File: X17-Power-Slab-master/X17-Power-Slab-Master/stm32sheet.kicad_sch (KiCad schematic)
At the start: 18 parts, among them J1 61201021621, SW2 1825910-6, U4 STM32F091CCTx, U7 ABLS-8.000MHZ-B2-T

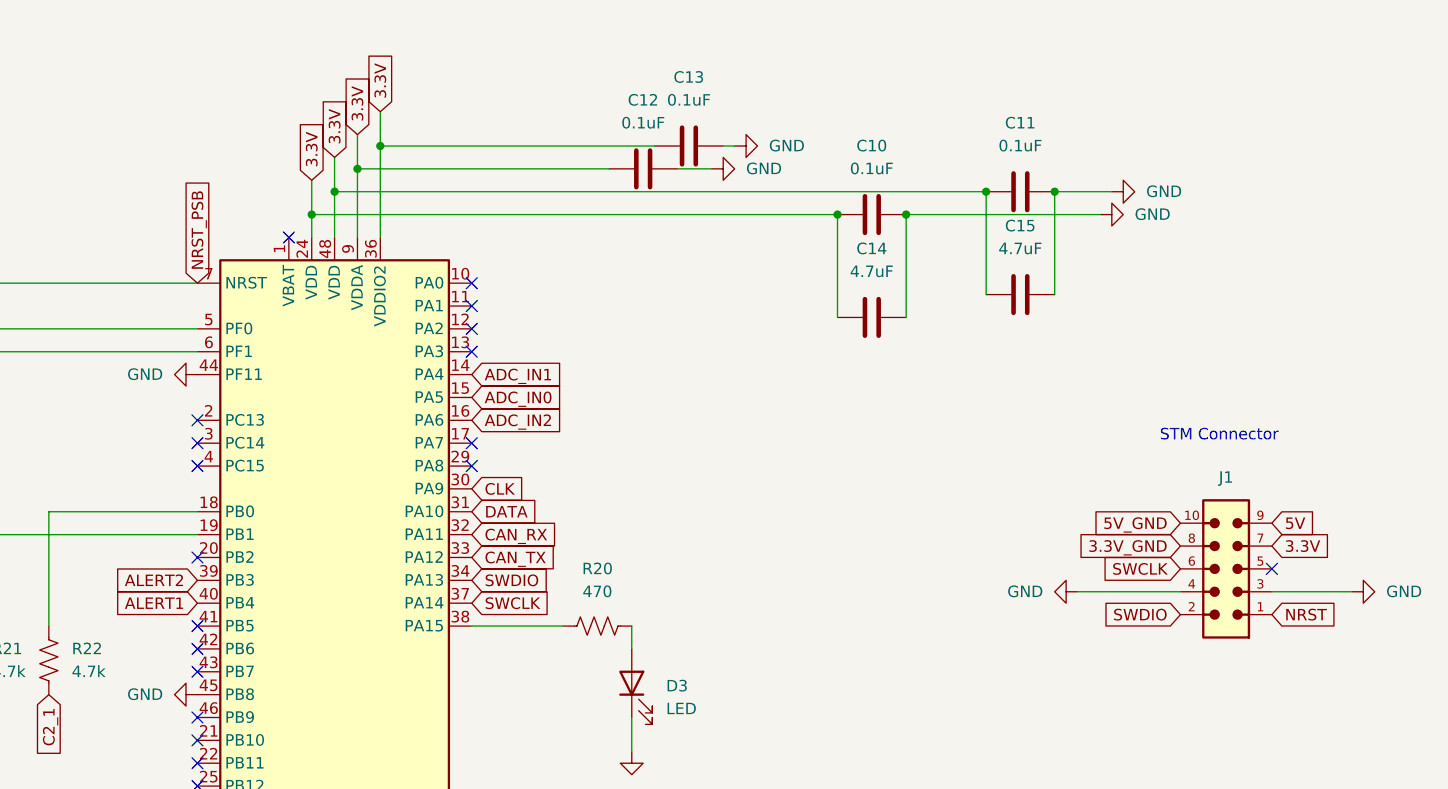
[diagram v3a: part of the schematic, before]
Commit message: Final First(?) Draft
NRST is stuck to general ground for whatever reason.

Test points wont connect for the life of me, will look @ in morning, will have sample plan.

Idea is there, really want to plan it out better 2nd time around. Alumni will give good tips!
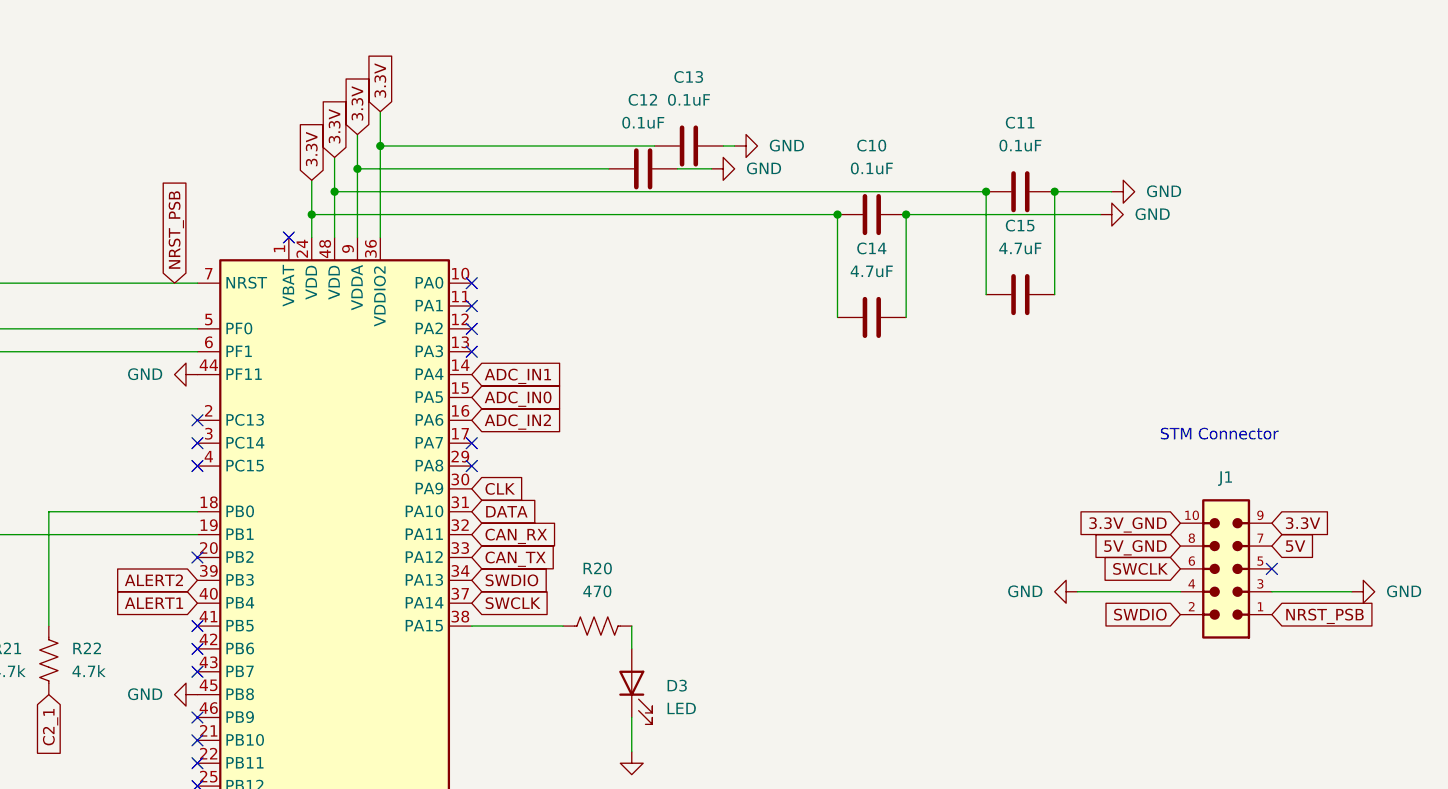
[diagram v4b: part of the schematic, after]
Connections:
- net NRST is gone; now on net GND: J1.1
- net 3.3V: now also J1.9; no longer J1.7
- net 3.3V_GND: now also J1.10; no longer J1.8
- net 5V: now also J1.7; no longer J1.9
- net 5V_GND: now also J1.8; no longer J1.10
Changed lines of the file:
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@@
 	(global_label "NRST_PSB"
 		(shape input)
-		(at 123.19 102.87 90)
-		(fields_autoplaced yes)
-		(effects
-			(font
-				(size 1.27 1.27)
-			)
-			(justify left)
-		)
-		(property "Intersheetrefs" "${INTERSHEET_REFS}"
-			(at 123.19 90.3901 90)
+		(at 120.65 102.87 90)
+		(fields_autoplaced yes)
+		(effects
+			(font
+				(size 1.27 1.27)
+			)
+			(justify left)
+		)
+		(property "Intersheetrefs" "${INTERSHEET_REFS}"
+			(at 120.65 90.3901 90)
 			(effects
 				(font
@@
 		)
 	)
+	(global_label "3.3V_GND"
+		(shape input)
+		(at 232.41 129.54 180)
+		(fields_autoplaced yes)
+		(effects
+			(font
+				(size 1.27 1.27)
+			)
+			(justify right)
+		)
+		(property "Intersheetrefs" "${INTERSHEET_REFS}"
+			(at 220.4743 129.54 0)
+			(effects
+				(font
+					(size 1.27 1.27)
+				)
+				(justify right)
+				(hide yes)
+			)
+		)
+	)
 	(global_label "5V_GND"
 		(shape input)
-		(at 232.41 129.54 180)
-		(fields_autoplaced yes)
-		(effects
-			(font
-				(size 1.27 1.27)
-			)
-			(justify right)
-		)
-		(property "Intersheetrefs" "${INTERSHEET_REFS}"
-			(at 222.2886 129.54 0)
-			(effects
-				(font
-					(size 1.27 1.27)
-				)
-				(justify right)
-				(hide yes)
-			)
-		)
-	)
-	(global_label "3.3V_GND"
-		(shape input)
 		(at 232.41 132.08 180)
 		(fields_autoplaced yes)
@@
 		)
 		(property "Intersheetrefs" "${INTERSHEET_REFS}"
-			(at 220.4743 132.08 0)
+			(at 222.2886 132.08 0)
 			(effects
 				(font
@@
 		)
 	)
-	(global_label "NRST"
+	(global_label "NRST_PSB"
 		(shape input)
 		(at 242.57 139.7 0)
@@
 		)
 		(property "Intersheetrefs" "${INTERSHEET_REFS}"
-			(at 250.3328 139.7 0)
+			(at 255.0499 139.7 0)
 			(effects
 				(font
@@
 		)
 	)
+	(global_label "3.3V"
+		(shape input)
+		(at 242.57 129.54 0)
+		(fields_autoplaced yes)
+		(effects
+			(font
+				(size 1.27 1.27)
+			)
+			(justify left)
+		)
+		(property "Intersheetrefs" "${INTERSHEET_REFS}"
+			(at 249.6676 129.54 0)
+			(effects
+				(font
+					(size 1.27 1.27)
+				)
+				(justify left)
+				(hide yes)
+			)
+		)
+	)
+	(global_label "3.3V"
+		(shape input)
+		(at 143.51 83.82 90)
+		(fields_autoplaced yes)
+		(effects
+			(font
+				(size 1.27 1.27)
+			)
+			(justify left)
+		)
+		(property "Intersheetrefs" "${INTERSHEET_REFS}"
+			(at 143.51 76.7224 90)
+			(effects
+				(font
+					(size 1.27 1.27)
+				)
+				(justify left)
+				(hide yes)
+			)
+		)
+	)
+	(global_label "3.3V"
+		(shape input)
+		(at 140.97 86.36 90)
+		(fields_autoplaced yes)
+		(effects
+			(font
+				(size 1.27 1.27)
+			)
+			(justify left)
+		)
+		(property "Intersheetrefs" "${INTERSHEET_REFS}"
+			(at 140.97 79.2624 90)
+			(effects
+				(font
+					(size 1.27 1.27)
+				)
+				(justify left)
+				(hide yes)
+			)
+		)
+	)
+	(global_label "ADC_IN0"
+		(shape input)
+		(at 153.67 115.57 0)
+		(fields_autoplaced yes)
+		(effects
+			(font
+				(size 1.27 1.27)
+			)
+			(justify left)
+		)
+		(property "Intersheetrefs" "${INTERSHEET_REFS}"
+			(at 164.3962 115.57 0)
+			(effects
+				(font
+					(size 1.27 1.27)
+				)
+				(justify left)
+				(hide yes)
+			)
+		)
+	)
+	(global_label "CAN_RX"
+		(shape input)
+		(at 153.67 130.81 0)
+		(fields_autoplaced yes)
+		(effects
+			(font
+				(size 1.27 1.27)
+			)
+			(justify left)
+		)
+		(property "Intersheetrefs" "${INTERSHEET_REFS}"
+			(at 163.7914 130.81 0)
+			(effects
+				(font
+					(size 1.27 1.27)
+				)
+				(justify left)
+				(hide yes)
+			)
+		)
+	)
+	(global_label "SWDIO"
+		(shape input)
+		(at 232.41 139.7 180)
+		(fields_autoplaced yes)
+		(effects
+			(font
+				(size 1.27 1.27)
+			)
+			(justify right)
+		)
+		(property "Intersheetrefs" "${INTERSHEET_REFS}"
+			(at 223.5586 139.7 0)
+			(effects
+				(font
+					(size 1.27 1.27)
+				)
+				(justify right)
+				(hide yes)
+			)
+		)
+	)
 	(global_label "5V"
 		(shape input)
-		(at 242.57 129.54 0)
-		(fields_autoplaced yes)
-		(effects
-			(font
-				(size 1.27 1.27)
-			)
-			(justify left)
-		)
-		(property "Intersheetrefs" "${INTERSHEET_REFS}"
-			(at 247.8533 129.54 0)
-			(effects
-				(font
-					(size 1.27 1.27)
-				)
-				(justify left)
-				(hide yes)
-			)
-		)
-	)
-	(global_label "3.3V"
-		(shape input)
-		(at 143.51 83.82 90)
-		(fields_autoplaced yes)
-		(effects
-			(font
-				(size 1.27 1.27)
-			)
-			(justify left)
-		)
-		(property "Intersheetrefs" "${INTERSHEET_REFS}"
-			(at 143.51 76.7224 90)
-			(effects
-				(font
-					(size 1.27 1.27)
-				)
-				(justify left)
-				(hide yes)
-			)
-		)
-	)
-	(global_label "3.3V"
-		(shape input)
-		(at 140.97 86.36 90)
-		(fields_autoplaced yes)
-		(effects
-			(font
-				(size 1.27 1.27)
-			)
-			(justify left)
-		)
-		(property "Intersheetrefs" "${INTERSHEET_REFS}"
-			(at 140.97 79.2624 90)
-			(effects
-				(font
-					(size 1.27 1.27)
-				)
-				(justify left)
-				(hide yes)
-			)
-		)
-	)
-	(global_label "ADC_IN0"
-		(shape input)
-		(at 153.67 115.57 0)
-		(fields_autoplaced yes)
-		(effects
-			(font
-				(size 1.27 1.27)
-			)
-			(justify left)
-		)
-		(property "Intersheetrefs" "${INTERSHEET_REFS}"
-			(at 164.3962 115.57 0)
-			(effects
-				(font
-					(size 1.27 1.27)
-				)
-				(justify left)
-				(hide yes)
-			)
-		)
-	)
-	(global_label "CAN_RX"
-		(shape input)
-		(at 153.67 130.81 0)
-		(fields_autoplaced yes)
-		(effects
-			(font
-				(size 1.27 1.27)
-			)
-			(justify left)
-		)
-		(property "Intersheetrefs" "${INTERSHEET_REFS}"
-			(at 163.7914 130.81 0)
-			(effects
-				(font
-					(size 1.27 1.27)
-				)
-				(justify left)
-				(hide yes)
-			)
-		)
-	)
-	(global_label "SWDIO"
-		(shape input)
-		(at 232.41 139.7 180)
-		(fields_autoplaced yes)
-		(effects
-			(font
-				(size 1.27 1.27)
-			)
-			(justify right)
-		)
-		(property "Intersheetrefs" "${INTERSHEET_REFS}"
-			(at 223.5586 139.7 0)
-			(effects
-				(font
-					(size 1.27 1.27)
-				)
-				(justify right)
-				(hide yes)
-			)
-		)
-	)
-	(global_label "3.3V"
-		(shape input)
 		(at 242.57 132.08 0)
 		(fields_autoplaced yes)
@@
 		)
 		(property "Intersheetrefs" "${INTERSHEET_REFS}"
-			(at 249.6676 132.08 0)
-			(effects
-				(font
+			(at 247.8533 132.08 0)
+			(effects
+				(font
